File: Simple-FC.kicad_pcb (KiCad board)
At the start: 2 copper layers, 40 x 40 mm, 73 parts, among them J1 USB_C_Receptacle_USB2.0_14P, J2 Micro_SD_Card, J3 Conn_01x04, J4 Conn_01x04, J5 Conn_01x04, J6 Conn_01x05, J7 Conn_01x04, J8 Conn_01x03, SW1 SW_Push, U1 RP2350A, U2 MMC5983MA, U3 LSM6DSM, U4 BMP384, U5 TPS631000, U6 W25Q128JVS, Y1 ABM8-272-T3

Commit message: drafted pcb layout
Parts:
- added D2: D_Schottky, Diode_SMD:D_0402_1005Metric, F.Cu at (83.2, 94.0)
- added J10: Conn_01x01, Connector_Wire:SolderWirePad_1x01_SMD_1x2mm, F.Cu at (137.1, 123.0)
- added J9: Conn_01x01, Connector_Wire:SolderWirePad_1x01_SMD_1x2mm, F.Cu at (134.5, 123.0)
- J2: moved to F.Cu
- J3, J7: footprint Connector_JST:JST_XH_B4B-XH-A_1x04_P2.50mm_Vertical -> Connector_PinHeader_2.54mm:PinHeader_1x04_P2.54mm_Vertical
- J4: footprint Connector_JST:JST_XH_B4B-XH-A_1x04_P2.50mm_Vertical -> Connector_PinSocket_2.54mm:PinSocket_1x04_P2.54mm_Vertical; moved to F.Cu
- J5: footprint Connector_JST:JST_XH_B4B-XH-A_1x04_P2.50mm_Vertical -> Connector_PinHeader_2.54mm:PinHeader_1x04_P2.54mm_Vertical; moved to F.Cu
- J8: footprint Connector_JST:JST_XH_B3B-XH-A_1x03_P2.50mm_Vertical -> Connector_PinHeader_2.54mm:PinHeader_1x03_P2.54mm_Vertical
- L1, L2: footprint Package_TO_SOT_SMD:SOT-583-8 -> Inductor_SMD:L_0805_2012Metric
- moved U4 94.3 mm to (155.7, 102.8)
- moved U3 93.8 mm to (154.5, 108.5)
- moved U6 90.1 mm to (143.5, 97.5)
- moved Y1 83.1 mm to (150.0, 110.0)
- moved U5 73.3 mm to (156.8, 96.8)
- moved U2 72.6 mm to (134.8, 115.7)
- moved SW1 71.5 mm to (133.5, 107.0)
- moved J8 60.0 mm to (134.0, 98.0), turned to 180 degrees
- moved J6 46.6 mm to (134.4, 87.0), turned to 90 degrees
- moved J1 13.5 mm to (152.5, 87.5)
- moved J3 12.1 mm to (163.0, 95.7), turned to 0 degrees
- moved J5 12.1 mm to (127.0, 95.7), turned to 0 degrees
- moved L1 7.68 mm to (77.4, 85.5)
- moved L2 7.68 mm to (81.1, 85.5)
- moved J4 5.11 mm to (163.0, 107.0), turned to 0 degrees
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
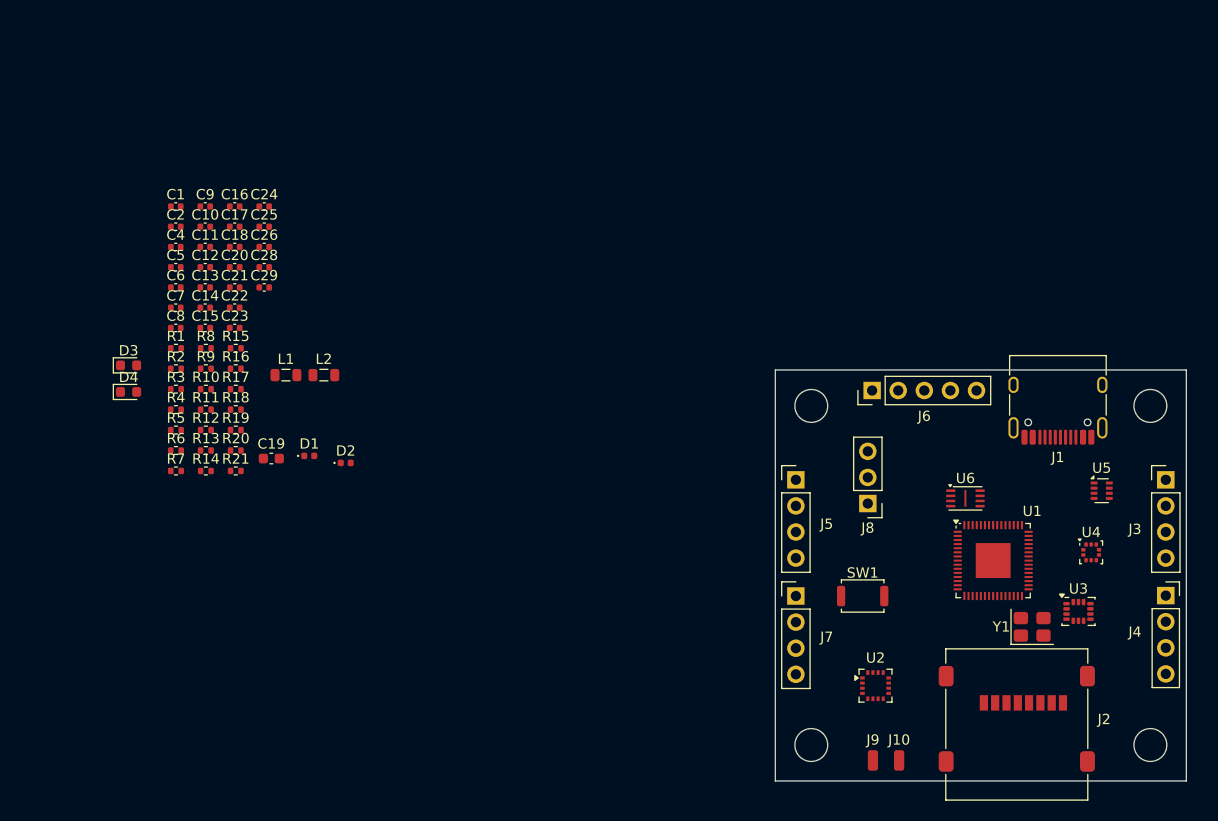
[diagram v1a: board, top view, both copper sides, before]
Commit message: routed mcu and power on pcb
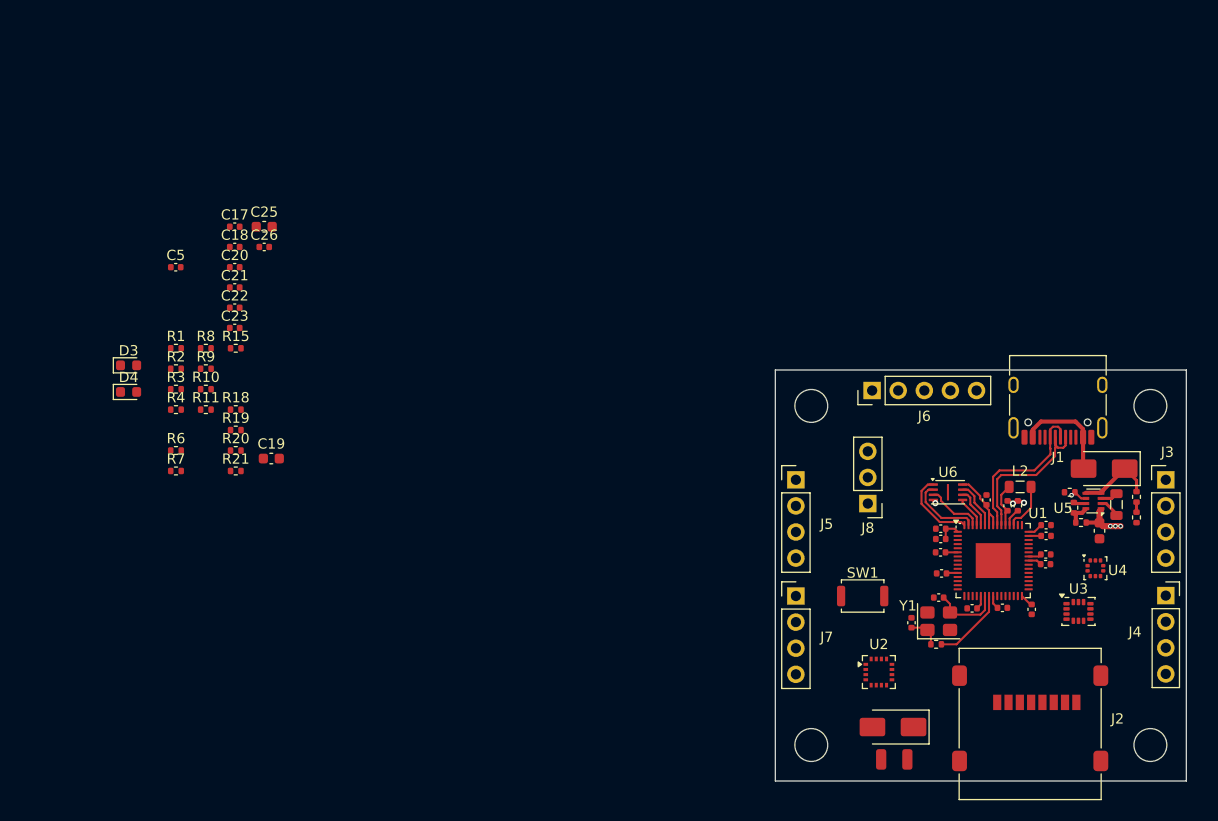
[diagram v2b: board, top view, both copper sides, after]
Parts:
- C24, C25: footprint Capacitor_SMD:C_0402_1005Metric -> Capacitor_SMD:C_0603_1608Metric
- D1, D2: footprint Diode_SMD:D_0402_1005Metric -> Diode_SMD:D_SMA
- moved R17 88.5 mm to (160.2, 99.3), turned to -90 degrees
- moved R16 88.5 mm to (160.2, 97.3), turned to -90 degrees
- moved C6 88.1 mm to (151.3, 101.2)
- moved C9 87.5 mm to (151.3, 100.1)
- moved C24 87.2 mm to (156.6, 100.7), turned to -90 degrees
- moved C12 86.4 mm to (151.3, 103.0)
- moved C13 86.3 mm to (149.9, 108.3), turned to -90 degrees
- moved C10 86.0 mm to (147.1, 108.2)
- moved R12 85.6 mm to (154.8, 99.8), turned to 180 degrees
- moved C15 85.0 mm to (151.3, 103.9)
- moved R13 84.7 mm to (154.1, 98.4), turned to 90 degrees
- moved R14 84.1 mm to (153.7, 96.9), turned to 180 degrees
- moved C1 83.4 mm to (140.9, 107.2)
- moved L1 81.8 mm to (158.2, 98.1), turned to -90 degrees
- moved C2 81.3 mm to (138.2, 109.6), turned to 90 degrees
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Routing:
- net +3V3: track 0.00 -> 23.3 mm, vias 0 -> 3
- net /USB_D-: track 0.00 -> 15.8 mm
- net /USB_D+: track 0.00 -> 15.8 mm
- net Net-(D1-A): track 0.00 -> 10.1 mm
- net +1V1: track 0.00 -> 8.19 mm
- net VBUS: track 0.00 -> 7.80 mm
- net /QSPI_SS: track 0.00 -> 7.70 mm
- net /XOUT: track 0.00 -> 7.48 mm
- net /QSPI_SD1: track 0.00 -> 7.19 mm
- net /XIN: track 0.00 -> 6.74 mm
- net /QSPI_SD2: track 0.00 -> 5.60 mm
- net Net-(U1-VREG_LX): track 0.00 -> 4.71 mm
- net /QSPI_SD3: track 0.00 -> 4.66 mm
- net /QSPI_SCLK: track 0.00 -> 3.96 mm
- net GND: track 0.00 -> 3.50 mm, vias 0 -> 3
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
